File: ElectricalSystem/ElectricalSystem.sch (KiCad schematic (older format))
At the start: 12 parts

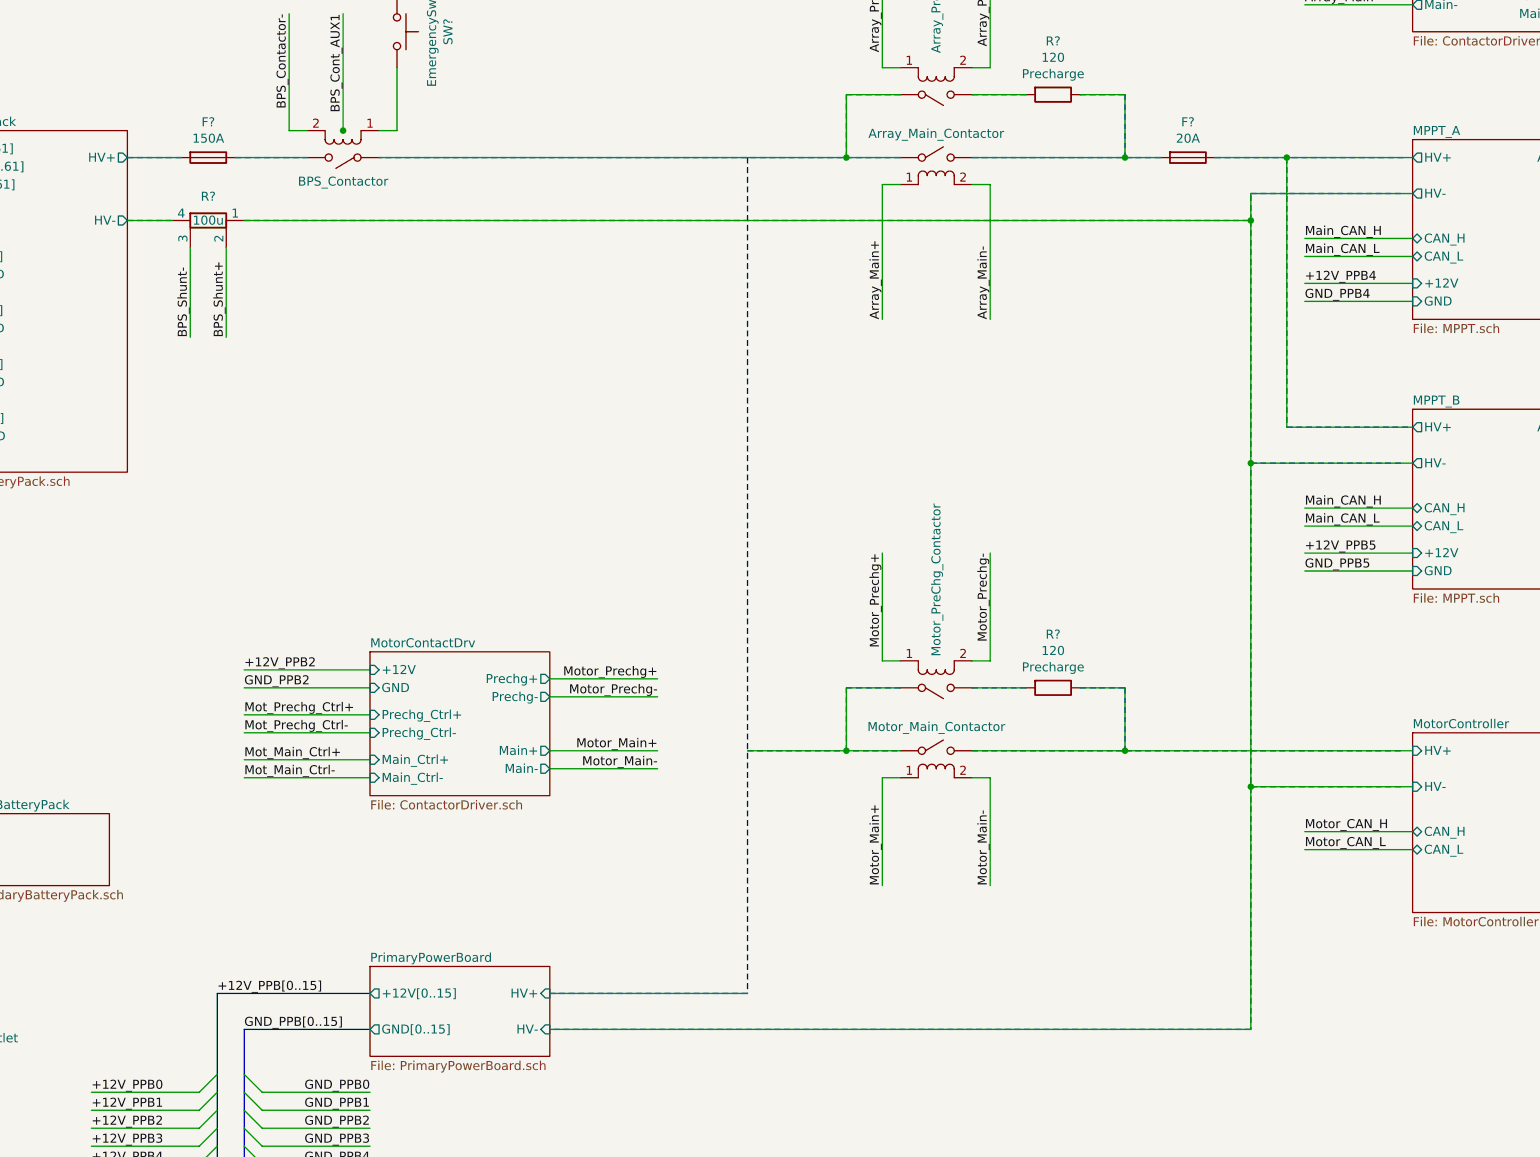
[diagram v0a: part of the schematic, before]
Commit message: adds new contactors for isolation
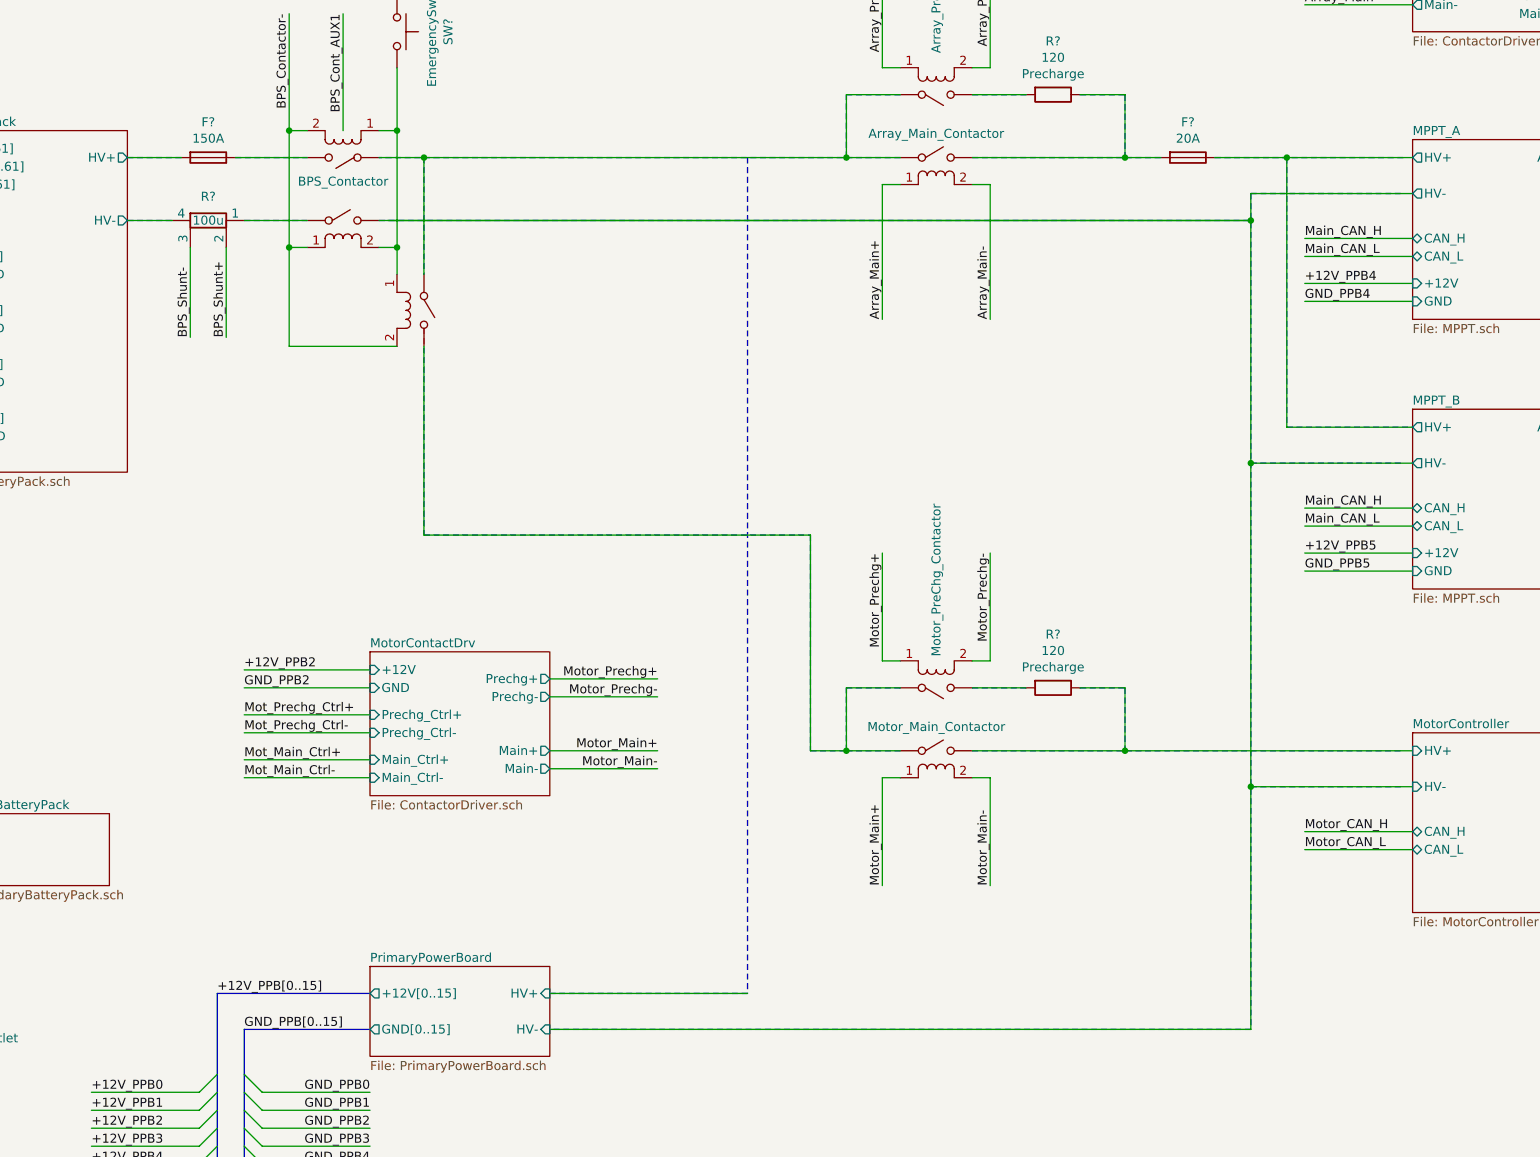
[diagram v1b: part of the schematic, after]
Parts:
- added U? (x2): BPS_Contactor, symbol UTSVT-ElectricalSystem:Contactor
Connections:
- net BPS_Contactor-: now also U?.1, U?.2
- net MPPT_A/HV-: now also U?.~; no longer R?.1
- net at SW?.2, U?.1: now also U?.1, U?.2
- net at U?.~: now also R?.2; no longer U?.~
- new net: U?.~, U?.~, U?.~, U?.~
- new net: R?.1, U?.~
- new net: U?.~, U?.~, U?.~
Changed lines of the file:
@@
 	-1   0    0    1
 $EndComp
-$Comp
-L Device:R_Shunt R?
-U 1 1 5F9A0FFC
-P 8500 3350
-F 0 "R?" V 8367 3350 50  0000 C CNN
-F 1 "100u" V 8500 3350 50  0000 C CNN
-F 2 "" V 8430 3350 50  0001 C CNN
-F 3 "~" H 8500 3350 50  0001 C CNN
-	1    8500 3350
-	0    1    1    0
-$EndComp
-Wire Wire Line
-	8300 3350 8050 3350
 Wire Wire Line
 	8400 3500 8400 4000
@@
 Wire Wire Line
 	12350 3150 12250 3150
-Connection ~ 14300 3350
 Connection ~ 12050 3000
 $Comp
@@
 F5 "CAN_L" B L 15200 6850 50
 $EndSheet
-Wire Wire Line
-	14300 3200 14300 3350
-Wire Wire Line
-	15200 3200 14300 3200
 Wire Wire Line
 	14500 3000 15200 3000
@@
 Wire Notes Line width 20 style solid rgb(255, 0, 0)
 	13600 5950 13600 6300
-Connection ~ 12050 6300
 Wire Wire Line
 	12050 5950 12350 5950
@@
 Wire Wire Line
 	12350 6300 12050 6300
-Wire Wire Line
-	11500 6300 12050 6300
-Wire Notes Line width 20 style solid rgb(255, 0, 0)
-	11500 6300 12350 6300
-Wire Notes Line width 20 style solid rgb(255, 0, 0)
-	12050 6300 12050 5950
 Wire Notes Line width 20 style solid rgb(255, 0, 0)
 	12050 5950 12350 5950
@@
 Wire Notes Line width 20 style solid rgb(255, 0, 0)
 	12750 6300 15150 6300
-Wire Notes Line width 20 style solid rgb(0, 0, 0)
-	8050 3350 8300 3350
-Wire Notes Line width 20 style solid rgb(0, 0, 0)
-	14300 3350 14300 3200
 Wire Notes Line width 20 style solid rgb(0, 0, 0)
 	14300 3200 15150 3200
 Wire Notes Line width 20 style solid rgb(0, 0, 0)
-	14300 3350 14300 7850
-Wire Notes Line width 20 style solid rgb(0, 0, 0)
 	14300 7850 10400 7850
-Wire Wire Line
-	14300 3350 14300 4700
 Wire Wire Line
 	15200 4700 14300 4700
@@
 	8350 3000 8050 3000
 Wire Wire Line
-	8700 3350 14300 3350
-Wire Notes Line width 20 style solid rgb(0, 0, 0)
-	8700 3350 14300 3350
-Wire Wire Line
 	9050 3000 8650 3000
-Wire Wire Line
-	9450 3000 12050 3000
 Wire Notes Line width 20 style solid rgb(255, 0, 0)
 	12350 3000 9450 3000
@@
 Wire Wire Line
 	9250 2200 9250 2850
+$Comp
+L UTSVT-ElectricalSystem:Contactor U?
+U 1 1 615CB386
+P 9250 3250
+F 0 "U?" H 9250 3400 50  0001 C CNN
+F 1 "BPS_Contactor" H 9250 3283 50  0001 C CNN
+F 2 "" H 9250 3250 50  0001 C CNN
+F 3 "" H 9250 3250 50  0001 C CNN
+	1    9250 3250
+	1    0    0    -1
+$EndComp
+$Comp
+L Device:R_Shunt R?
+U 1 1 5F9A0FFC
+P 8500 3350
+F 0 "R?" V 8367 3350 50  0000 C CNN
+F 1 "100u" V 8500 3350 50  0000 C CNN
+F 2 "" V 8430 3350 50  0001 C CNN
+F 3 "~" H 8500 3350 50  0001 C CNN
+	1    8500 3350
+	0    1    1    0
+$EndComp
+Wire Notes Line width 20 style solid rgb(0, 0, 0)
+	14300 3200 14300 7850
+Connection ~ 8950 2850
+Wire Wire Line
+	8950 3500 9050 3500
+Wire Wire Line
+	8950 2850 8950 3500
+Wire Wire Line
+	9550 2850 9550 3500
+Wire Wire Line
+	9550 3500 9450 3500
+Connection ~ 9550 2850
+$Comp
+L UTSVT-ElectricalSystem:Contactor U?
+U 1 1 61629C82
+P 9800 3850
+F 0 "U?" H 9800 4000 50  0001 C CNN
+F 1 "BPS_Contactor" H 9800 3883 50  0001 C CNN
+F 2 "" H 9800 3850 50  0001 C CNN
+F 3 "" H 9800 3850 50  0001 C CNN
+	1    9800 3850
+	0    1    1    0
+$EndComp
+Wire Wire Line
+	9550 3500 9550 3650
+Connection ~ 9550 3500
+Wire Wire Line
+	8950 3500 8950 4050
+Wire Wire Line
+	8950 4050 9550 4050
+Connection ~ 8950 3500
+Wire Wire Line
+	9700 5100 11850 5100
+Wire Wire Line
+	11850 5100 11850 6300
+Wire Wire Line
+	11850 6300 12050 6300
+Connection ~ 12050 6300
+Wire Notes Line width 20 style solid rgb(0, 0, 0)
+	8050 3350 8300 3350
+Wire Notes Line width 20 style solid rgb(0, 0, 0)
+	8700 3350 9050 3350
+Wire Notes Line width 20 style solid rgb(0, 0, 0)
+	9450 3350 14300 3350
+Wire Wire Line
+	14300 3200 14300 3350
+Connection ~ 14300 3350
+Wire Wire Line
+	14300 3350 14300 4700
+Wire Wire Line
+	14300 3200 15200 3200
+Wire Notes Line width 20 style solid rgb(255, 0, 0)
+	11850 5100 11850 6300
+Wire Notes Line width 20 style solid rgb(255, 0, 0)
+	11850 6300 12050 6300
+Wire Notes Line width 20 style solid rgb(255, 0, 0)
+	12050 6300 12050 5950
+Wire Wire Line
+	9450 3000 9700 3000
+Wire Wire Line
+	9700 3000 9700 3650
+Connection ~ 9700 3000
+Wire Wire Line
+	9700 3000 12050 3000
+Wire Notes Line width 20 style solid rgb(255, 0, 0)
+	9700 3000 9700 3650
+Wire Notes Line width 20 style solid rgb(255, 0, 0)
+	12050 6300 12350 6300
+Wire Wire Line
+	8700 3350 9050 3350
+Wire Wire Line
+	9500 3350 14300 3350
+Wire Wire Line
+	9450 3350 14300 3350
+Wire Wire Line
+	8050 3350 8300 3350
+Wire Notes Line width 20 style solid rgb(255, 0, 0)
+	9700 5100 11850 5100
 Wire Bus Line
 	8700 7850 8700 9800
 Wire Bus Line
 	8550 7650 8550 9800
-Connection ~ 9250 2850
+Wire Notes Line width 20 style solid rgb(255, 0, 0)
+	9700 3950 9700 5100
+Wire Wire Line
+	9700 4050 9700 5100
 $EndSCHEMATC

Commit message: updates for PVDR
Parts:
- removed U?: Motor_PreChg_Contactor, symbol UTSVT-ElectricalSystem:Contactor
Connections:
- new net: U?.~, U?.~, U?.~, U?.~
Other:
- moved on the sheet: F?, J?, R?, SW?
